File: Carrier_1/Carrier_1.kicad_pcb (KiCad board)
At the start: 2 copper layers, 31.5 x 20.8 mm, 3 parts, among them J1 Chubut_2 connector, U1 LGAD_2_pad

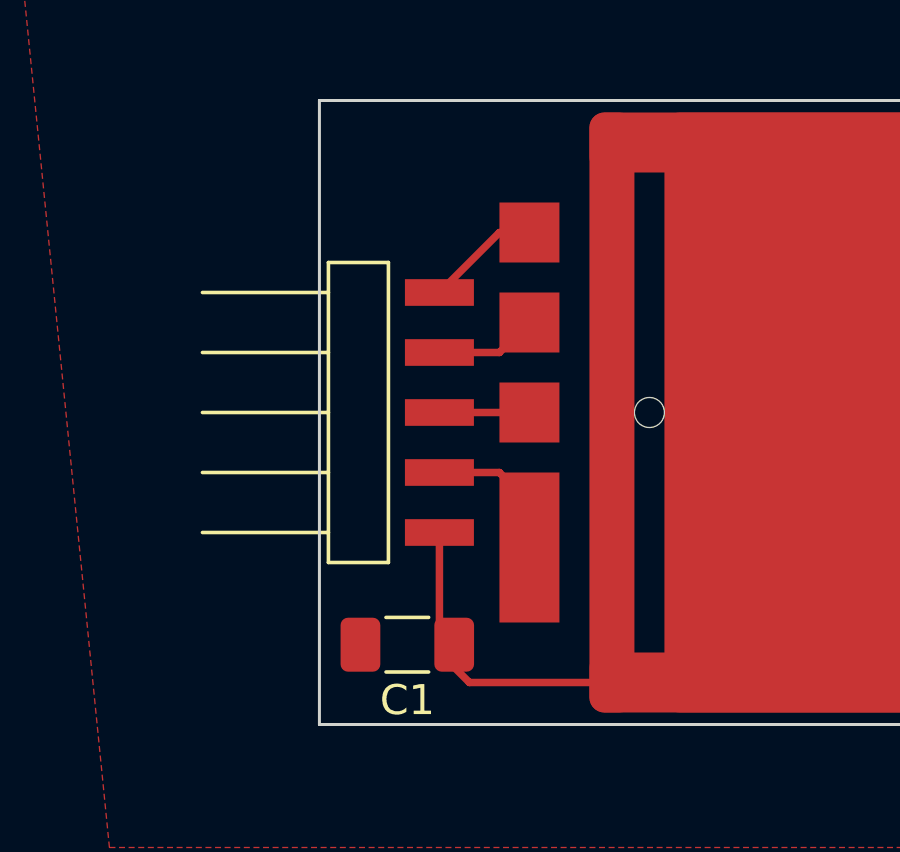
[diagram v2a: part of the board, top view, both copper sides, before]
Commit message: Slight changes in the carrier board, added title, date, author to the pages
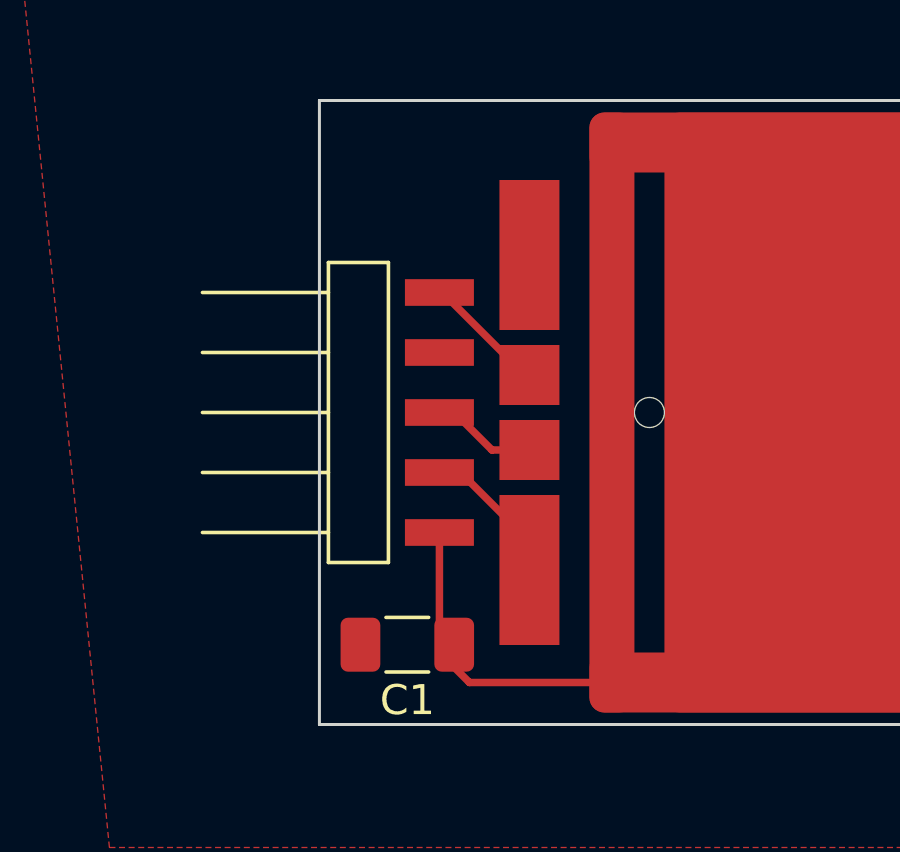
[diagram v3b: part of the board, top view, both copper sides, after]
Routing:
- net GND: track 8.33 -> 4.91 mm
- net Net-(J1-Pad3): track 3.00 -> 3.52 mm
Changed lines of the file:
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@@
     (thickness 1.6)
   )
-  (paper "A4")
+  (paper "A4" portrait)
+  (title_block
+    (title "LGAD carrier board compatible with Chubut 2")
+    (date "2022-07-20")
+    (company "Universität Zürich")
+    (comment 1 "Matias Senger")
+  )
   (layers
     (0 "F.Cu" signal)
@@
   )
   (setup
+    (stackup
+      (layer "F.SilkS" (type "Top Silk Screen"))
+      (layer "F.Paste" (type "Top Solder Paste"))
+      (layer "F.Mask" (type "Top Solder Mask") (thickness 0.01))
+      (layer "F.Cu" (type "copper") (thickness 0.035))
+      (layer "dielectric 1" (type "core") (thickness 1.51) (material "FR4") (epsilon_r 4.5) (loss_tangent 0.02))
+      (layer "B.Cu" (type "copper") (thickness 0.035))
+      (layer "B.Mask" (type "Bottom Solder Mask") (thickness 0.01))
+      (layer "B.Paste" (type "Bottom Solder Paste"))
+      (layer "B.SilkS" (type "Bottom Silk Screen"))
+      (copper_finish "None")
+      (dielectric_constraints no)
+    )
     (pad_to_mask_clearance 0)
     (aux_axis_origin 114 92)
@@
       (outputformat 1)
       (mirror false)
-      (drillshape 1)
+      (drillshape 0)
       (scaleselection 1)
-      (outputdirectory "")
+      (outputdirectory "gerber")
     )
   )
@@
     )
     (pad "" np_thru_hole circle (at 4 0) (size 1 1) (drill 1) (layers F&B.Cu))
+    (pad "1" smd roundrect (at 12 9 90) (size 2 20) (layers "F.Cu" "F.Paste" "F.Mask") (roundrect_rratio 0.25)
+      (net 3 "Net-(C1-Pad1)") (pintype "unspecified"))
+    (pad "1" smd roundrect (at 13.25 0) (size 17.5 20) (layers "F.Cu" "F.Paste" "F.Mask") (roundrect_rratio 0.02857142857)
+      (net 3 "Net-(C1-Pad1)") (pintype "unspecified"))
     (pad "1" smd roundrect (at 2.75 0) (size 1.5 20) (layers "F.Cu" "F.Paste" "F.Mask") (roundrect_rratio 0.3333333333)
       (net 3 "Net-(C1-Pad1)") (pintype "unspecified"))
-    (pad "1" smd roundrect (at 13.25 0) (size 17.5 20) (layers "F.Cu" "F.Paste" "F.Mask") (roundrect_rratio 0.02857142857)
-      (net 3 "Net-(C1-Pad1)") (pintype "unspecified"))
     (pad "1" smd roundrect (at 12 -9 90) (size 2 20) (layers "F.Cu" "F.Paste" "F.Mask") (roundrect_rratio 0.25)
       (net 3 "Net-(C1-Pad1)") (pintype "unspecified"))
-    (pad "1" smd roundrect (at 12 9 90) (size 2 20) (layers "F.Cu" "F.Paste" "F.Mask") (roundrect_rratio 0.25)
-      (net 3 "Net-(C1-Pad1)") (pintype "unspecified"))
-    (pad "2" smd rect (at 0 -3) (size 2 2) (layers "F.Cu" "F.Paste" "F.Mask")
+    (pad "2" smd rect (at 0 5.25) (size 2 5) (layers "F.Cu" "F.Paste" "F.Mask")
       (net 1 "GND") (pintype "unspecified"))
-    (pad "2" smd rect (at 0 4.5) (size 2 5) (layers "F.Cu" "F.Paste" "F.Mask")
+    (pad "2" smd rect (at 0 -5.25) (size 2 5) (layers "F.Cu" "F.Paste" "F.Mask")
       (net 1 "GND") (pintype "unspecified"))
-    (pad "3" smd rect (at 0 0) (size 2 2) (layers "F.Cu" "F.Paste" "F.Mask")
+    (pad "3" smd rect (at 0 1.25) (size 2 2) (layers "F.Cu" "F.Paste" "F.Mask")
       (net 2 "Net-(J1-Pad3)") (pintype "unspecified"))
-    (pad "4" smd rect (at 0 -6) (size 2 2) (layers "F.Cu" "F.Paste" "F.Mask")
+    (pad "4" smd rect (at 0 -1.25) (size 2 2) (layers "F.Cu" "F.Paste" "F.Mask")
       (net 4 "Net-(J1-Pad1)") (pintype "unspecified"))
     (zone (net 0) (net_name "") (layers "F.Adhes" "F.Paste" "F.SilkS" "F.Mask" "F.CrtYd") (hatch edge 0.508)
@@
     (fp_line (start -1.6 -0.8) (end 1.6 -0.8) (layer "F.Fab") (width 0.1))
     (fp_line (start -1.6 0.8) (end -1.6 -0.8) (layer "F.Fab") (width 0.1))
-    (pad "1" smd roundrect (at -1.5625 0 180) (size 1.325 1.8) (layers "F.Cu" "F.Paste" "F.Mask") (roundrect_rratio 0.188679)
+    (pad "1" smd roundrect (at -1.5625 0 180) (size 1.325 1.8) (layers "F.Cu" "F.Paste" "F.Mask") (roundrect_rratio 0.1886792453)
       (net 3 "Net-(C1-Pad1)") (pintype "passive"))
-    (pad "2" smd roundrect (at 1.5625 0 180) (size 1.325 1.8) (layers "F.Cu" "F.Paste" "F.Mask") (roundrect_rratio 0.188679)
+    (pad "2" smd roundrect (at 1.5625 0 180) (size 1.325 1.8) (layers "F.Cu" "F.Paste" "F.Mask") (roundrect_rratio 0.1886792453)
       (net 1 "GND") (pintype "passive"))
     (model "${KICAD6_3DMODEL_DIR}/Capacitor_SMD.3dshapes/C_1206_3216Metric.wrl"
@@
   )
   (gr_rect (start 103 81.6) (end 134.5 102.4) (layer "Edge.Cuts") (width 0.1) (fill none))
-  (segment (start 107 90) (end 109 90) (width 0.25) (layer "F.Cu") (net 1))
-  (segment (start 109 94) (end 110 95) (width 0.25) (layer "F.Cu") (net 1))
-  (segment (start 110 95) (end 110 96.5) (width 0.25) (layer "F.Cu") (net 1))
-  (segment (start 107 94) (end 109 94) (width 0.25) (layer "F.Cu") (net 1))
-  (segment (start 109 90) (end 110 89) (width 0.25) (layer "F.Cu") (net 1))
-  (segment (start 110 92) (end 107 92) (width 0.25) (layer "F.Cu") (net 2))
+  (segment (start 110 96.295) (end 110 97.25) (width 0.25) (layer "F.Cu") (net 1))
+  (segment (start 107.705 94) (end 110 96.295) (width 0.25) (layer "F.Cu") (net 1))
+  (segment (start 107 94) (end 107.705 94) (width 0.25) (layer "F.Cu") (net 1))
+  (segment (start 107 92) (end 107.5 92) (width 0.25) (layer "F.Cu") (net 2))
+  (segment (start 107.5 92) (end 108.75 93.25) (width 0.25) (layer "F.Cu") (net 2))
+  (segment (start 108.75 93.25) (end 110 93.25) (width 0.25) (layer "F.Cu") (net 2))
   (segment (start 107 100) (end 108 101) (width 0.25) (layer "F.Cu") (net 3))
   (segment (start 107 96) (end 107 100) (width 0.25) (layer "F.Cu") (net 3))
   (segment (start 108 101) (end 122 101) (width 0.25) (layer "F.Cu") (net 3))
-  (segment (start 109 86) (end 110 86) (width 0.25) (layer "F.Cu") (net 4))
-  (segment (start 107 88) (end 109 86) (width 0.25) (layer "F.Cu") (net 4))
+  (segment (start 110 90.75) (end 109.85 90.75) (width 0.25) (layer "F.Cu") (net 4))
+  (segment (start 109.85 90.75) (end 107.1 88) (width 0.25) (layer "F.Cu") (net 4))
+  (segment (start 107.1 88) (end 107 88) (width 0.25) (layer "F.Cu") (net 4))
   (zone (net 1) (net_name "GND") (layer "F.Cu") (hatch edge 0.508)
     (connect_pads (clearance 0.508))

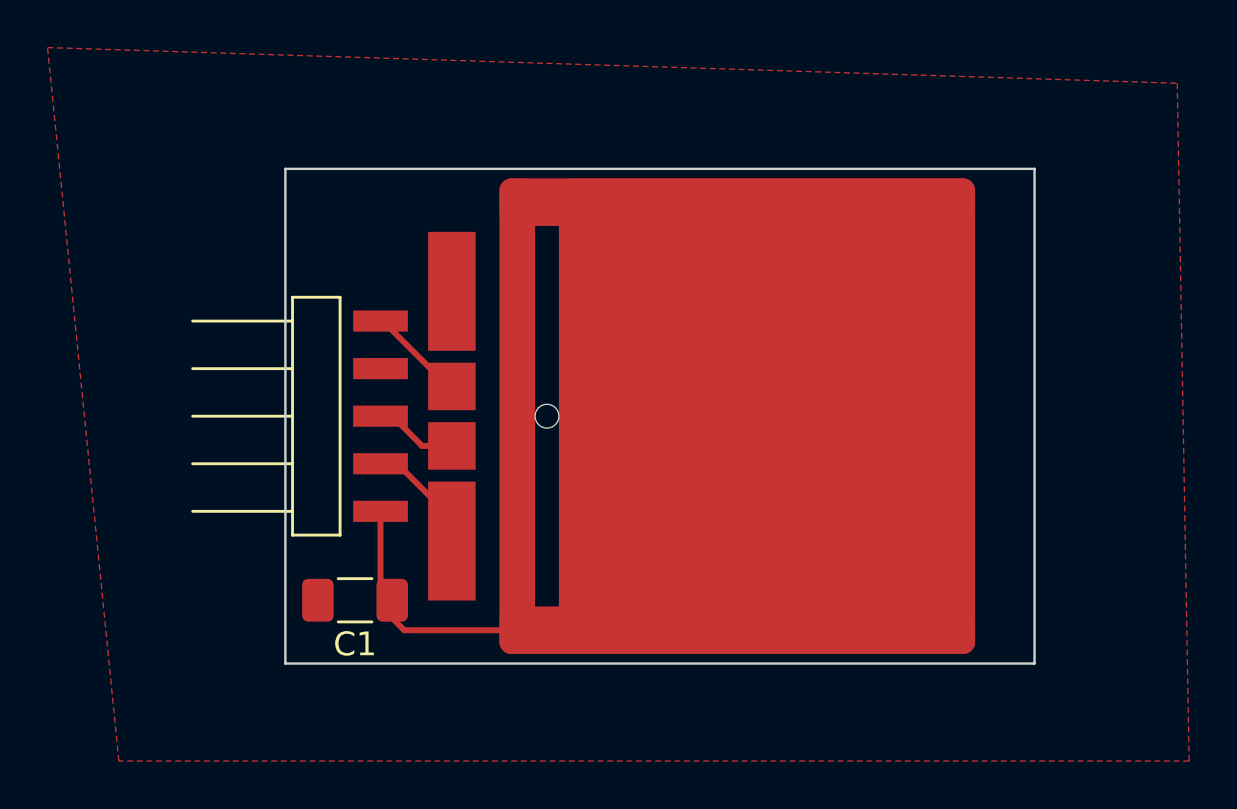
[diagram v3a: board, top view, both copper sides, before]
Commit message: "Money is not a problem here", so I changed to 4 layers of copper and fully RF shielded design
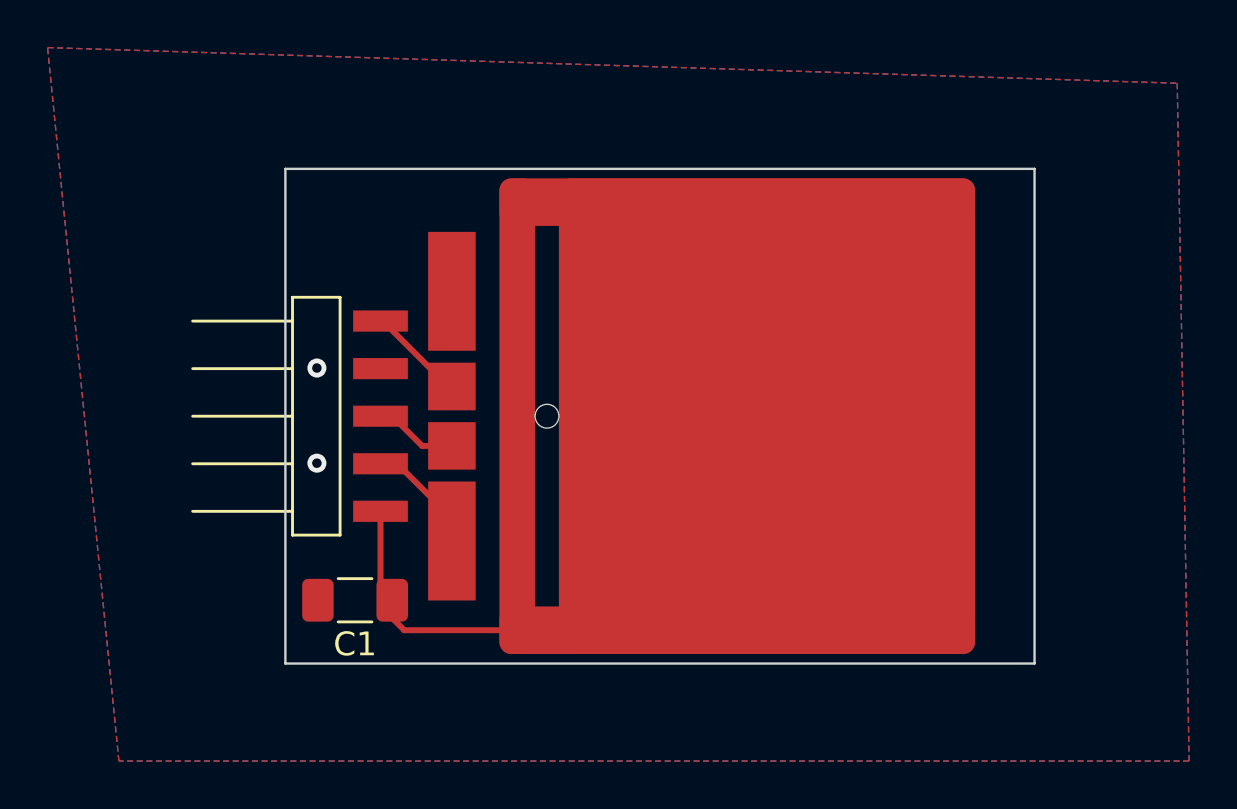
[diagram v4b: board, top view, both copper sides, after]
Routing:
- net GND: vias 0 -> 2
- added copper zone on B.Cu, net GND
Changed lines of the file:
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@@
   (segment (start 107.705 94) (end 110 96.295) (width 0.25) (layer "F.Cu") (net 1))
   (segment (start 107 94) (end 107.705 94) (width 0.25) (layer "F.Cu") (net 1))
+  (via (at 104.325 89.975) (size 0.8) (drill 0.4) (layers "F.Cu" "B.Cu") (free) (net 1))
+  (via (at 104.325 93.975) (size 0.8) (drill 0.4) (layers "F.Cu" "B.Cu") (free) (net 1))
   (segment (start 107 92) (end 107.5 92) (width 0.25) (layer "F.Cu") (net 2))
   (segment (start 107.5 92) (end 108.75 93.25) (width 0.25) (layer "F.Cu") (net 2))
@@
   (segment (start 109.85 90.75) (end 107.1 88) (width 0.25) (layer "F.Cu") (net 4))
   (segment (start 107.1 88) (end 107 88) (width 0.25) (layer "F.Cu") (net 4))
-  (zone (net 1) (net_name "GND") (layer "F.Cu") (hatch edge 0.508)
+  (zone (net 1) (net_name "GND") (layers F&B.Cu) (hatch edge 0.508)
     (connect_pads (clearance 0.508))
     (min_thickness 0.254) (filled_areas_thickness no)

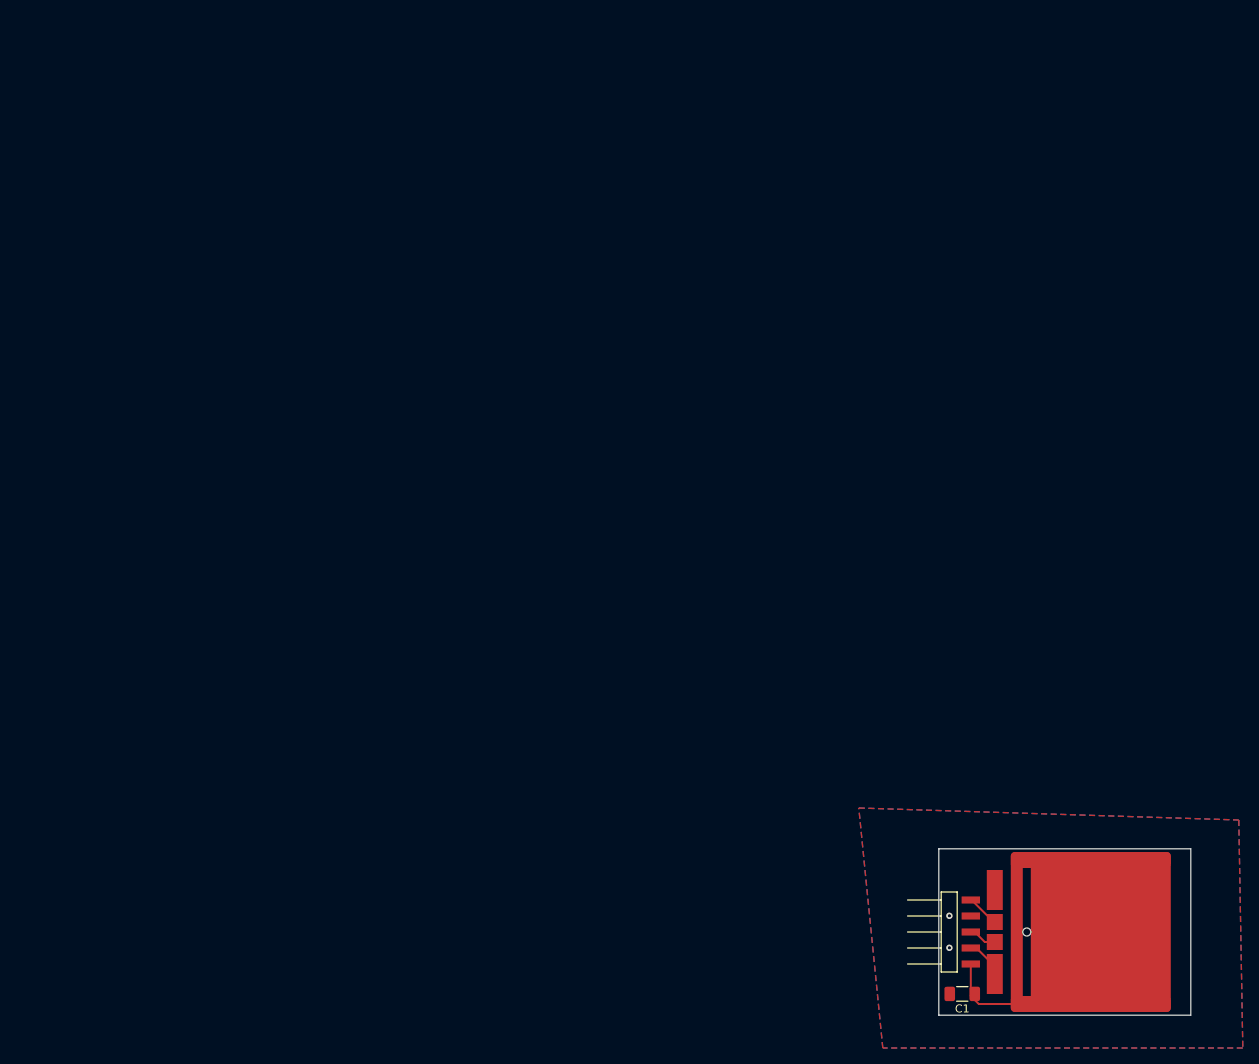
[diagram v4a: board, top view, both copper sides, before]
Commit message: New version with RF shield covering 100 % of the LGAD stuff
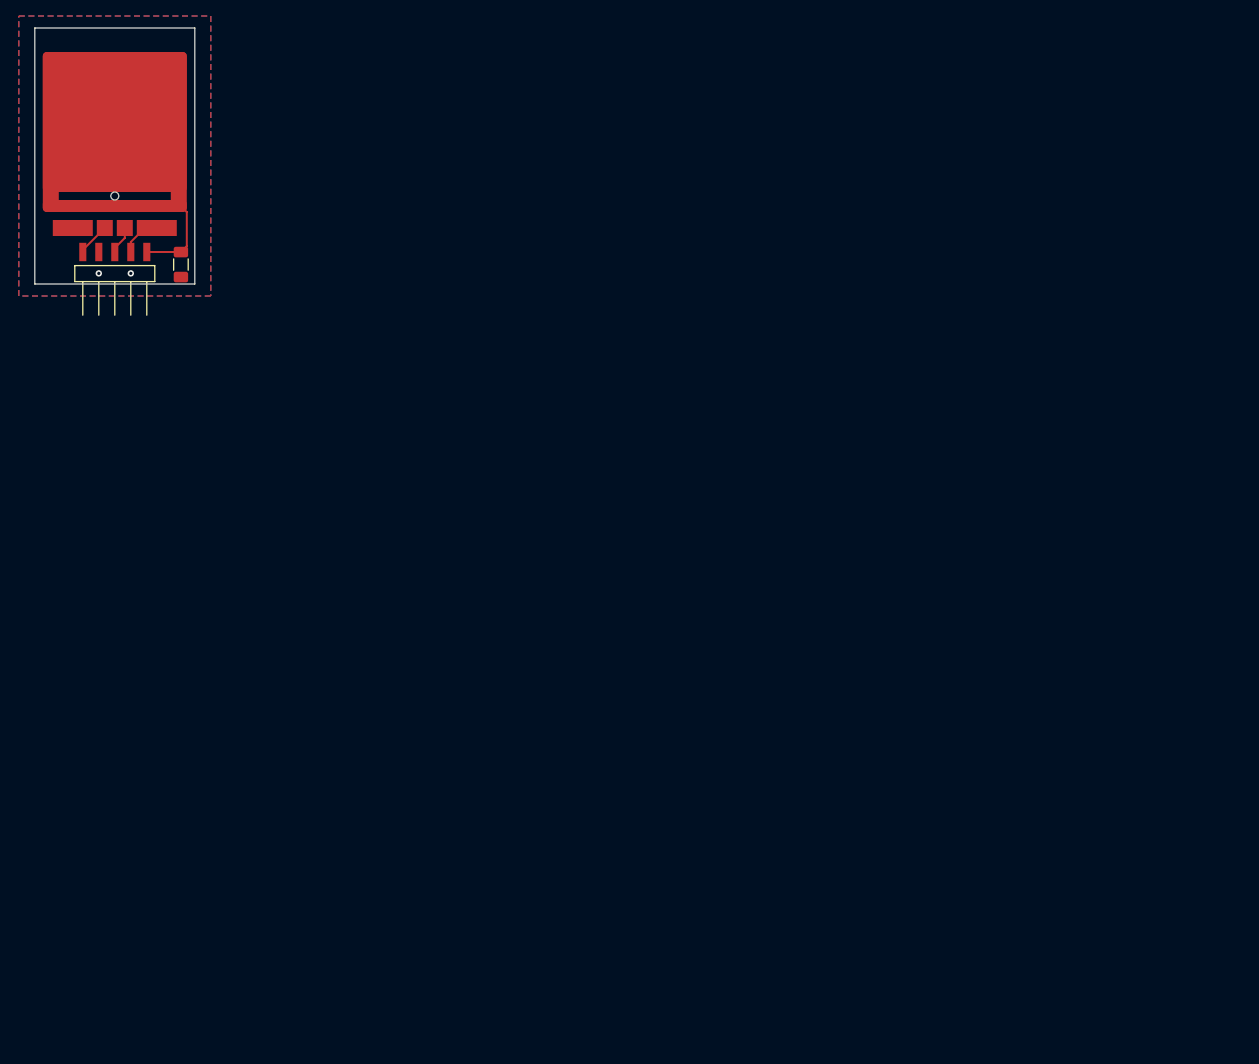
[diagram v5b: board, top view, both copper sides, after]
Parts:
- moved U1 143.4 mm to (0.00, 0.00)
- moved C1 133.6 mm to (8.27, 8.57), turned to -90 degrees
- moved J1 131.2 mm to (0.00, 7.00), turned to 90 degrees
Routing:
- net Net-(C1-Pad1): track 19.4 -> 18.9 mm
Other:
- board size 31.5 x 20.8 mm -> 20 x 32 mm
